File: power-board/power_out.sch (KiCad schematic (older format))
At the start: 10 parts, among them U2 TPS63001, U3 SiP32431DR3, U4 SiP32431DR3, U5 SiP32431DR3

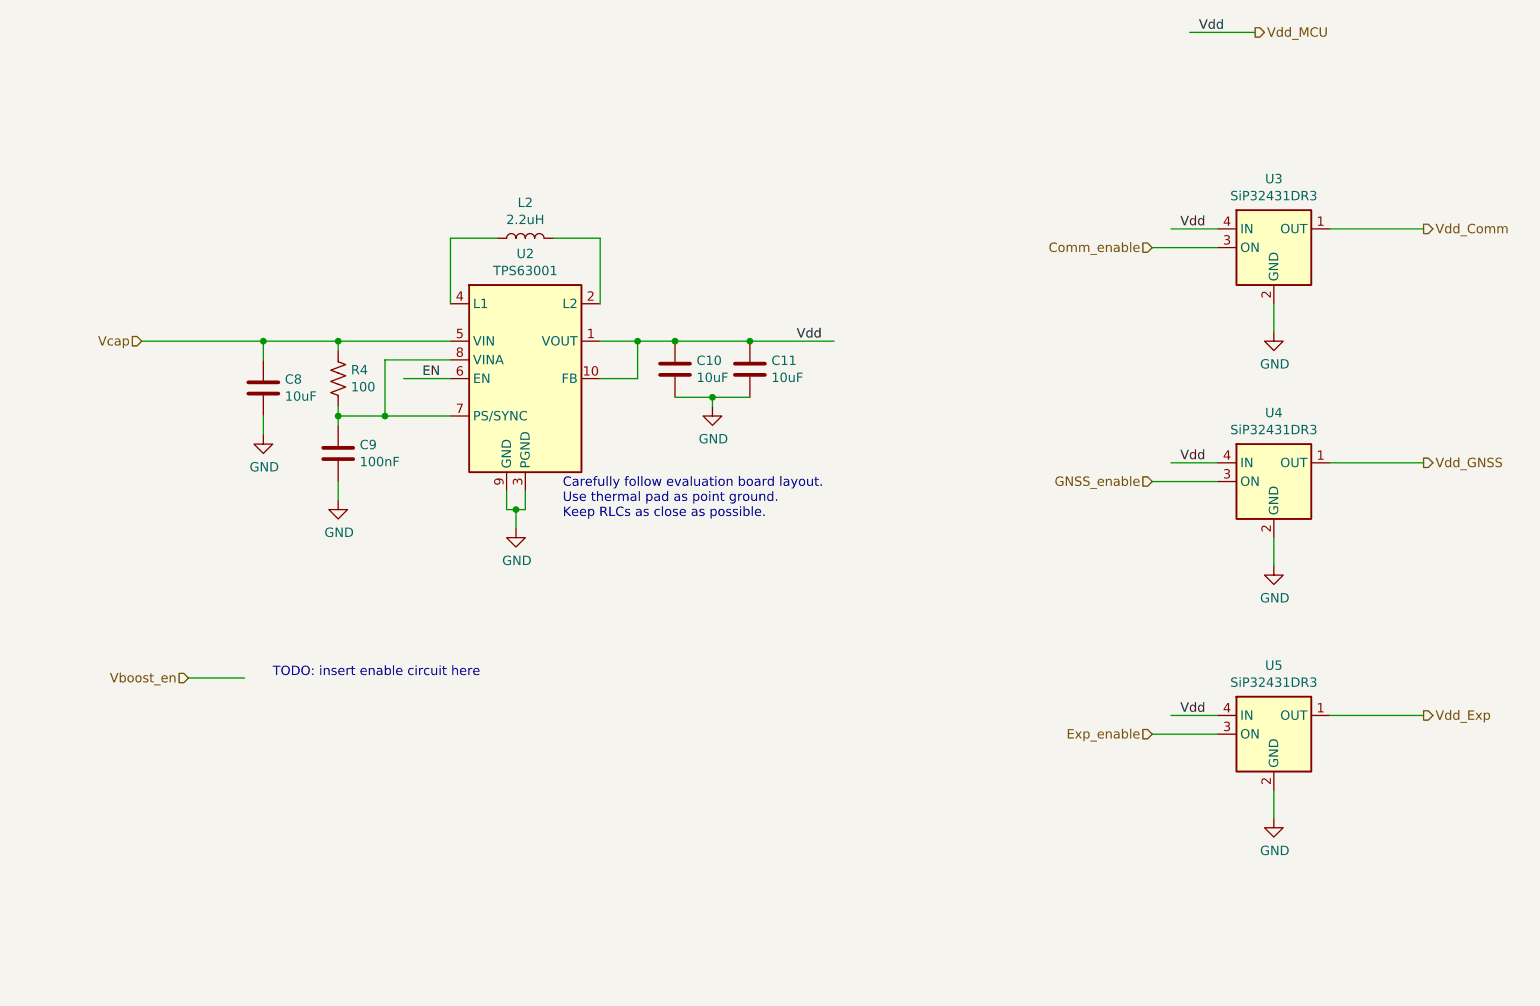
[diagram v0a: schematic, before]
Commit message: Updated schematics to reflect new resistor values
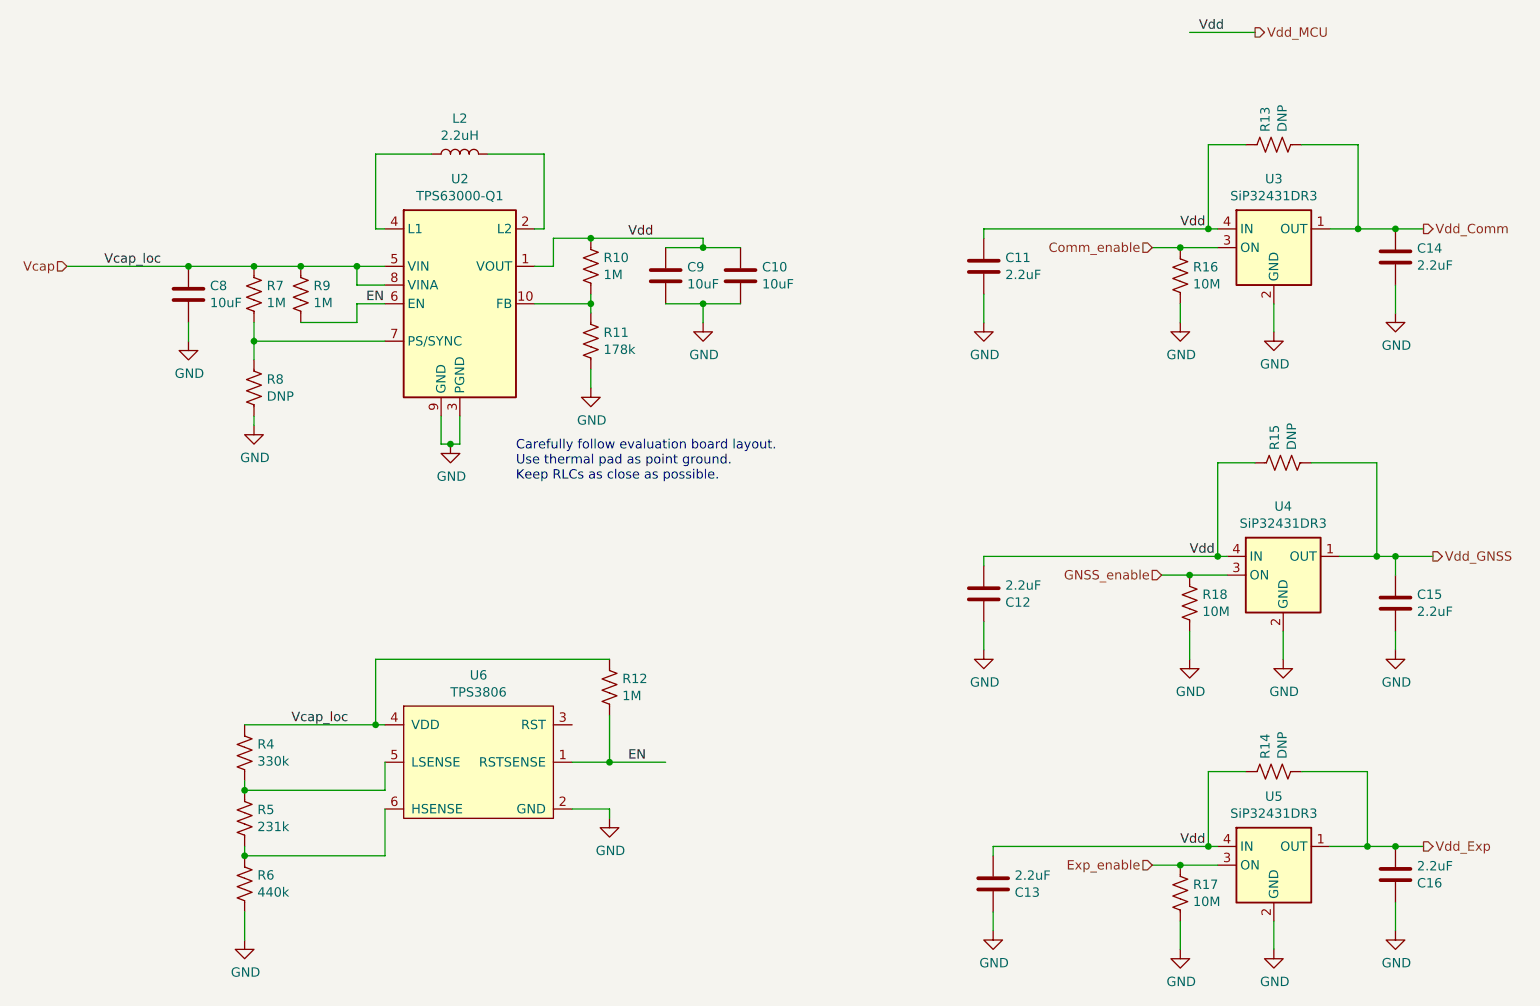
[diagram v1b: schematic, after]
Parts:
- removed U2: TPS63001, Package_SON:Texas_DRC0010J_ThermalVias, symbol Regulator_Switching:TPS63001
- added C12, C13, C14, C15, C16: 2.2uF, symbol Device:C
- added R10, R12, R7, R9: 1M, symbol Device:R_US
- added R11: 178k, symbol Device:R_US
- added R13, R14, R15, R8: DNP, symbol Device:R_US
- added R16, R17, R18: 10M, symbol Device:R_US
- added R5: 231k, symbol Device:R_US
- added R6: 440k, symbol Device:R_US
- added U2: TPS63000-Q1, Package_SON:Texas_DRC0010J_ThermalVias, symbol Regulator_Switching:TPS63000-Q1
- added U6: TPS3806, symbol power-board:TPS3806
- C11: value 10uF -> 2.2uF
- C9: value 100nF -> 10uF
- R4: value 100 -> 330k
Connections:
- net labels added: Vcap_loc
- net labels removed: Vboost_en
- wire segments 46 -> 105
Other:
- note removed: "TODO: insert enable circuit here"
- moved on the sheet: U4, U5
